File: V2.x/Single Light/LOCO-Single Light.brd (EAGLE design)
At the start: 25.1 x 16.8 mm, 49 parts, among them IC1 Atmega 328-P, IC2 MCP2515, IC3 MIC5219BM5, IC4 TP4056, IC5 DW01A, Q1 8MHz, Q2 16MHz, Q3 BSS123, Q4 FS8205ASOT-23-6L_TCP-L

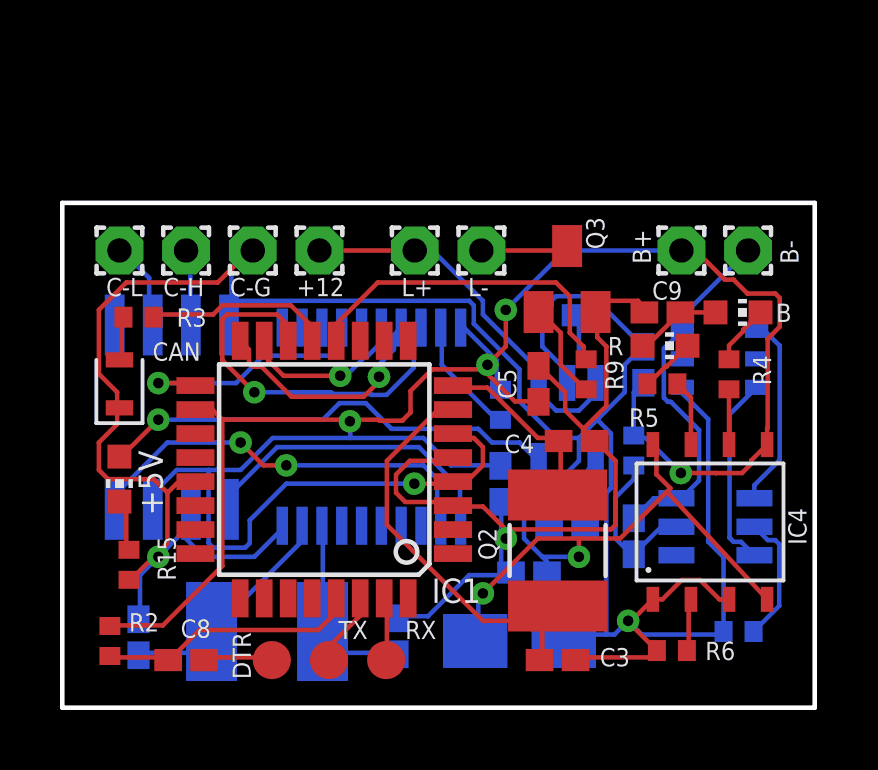
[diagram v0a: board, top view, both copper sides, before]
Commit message: new single light and single light akku versions
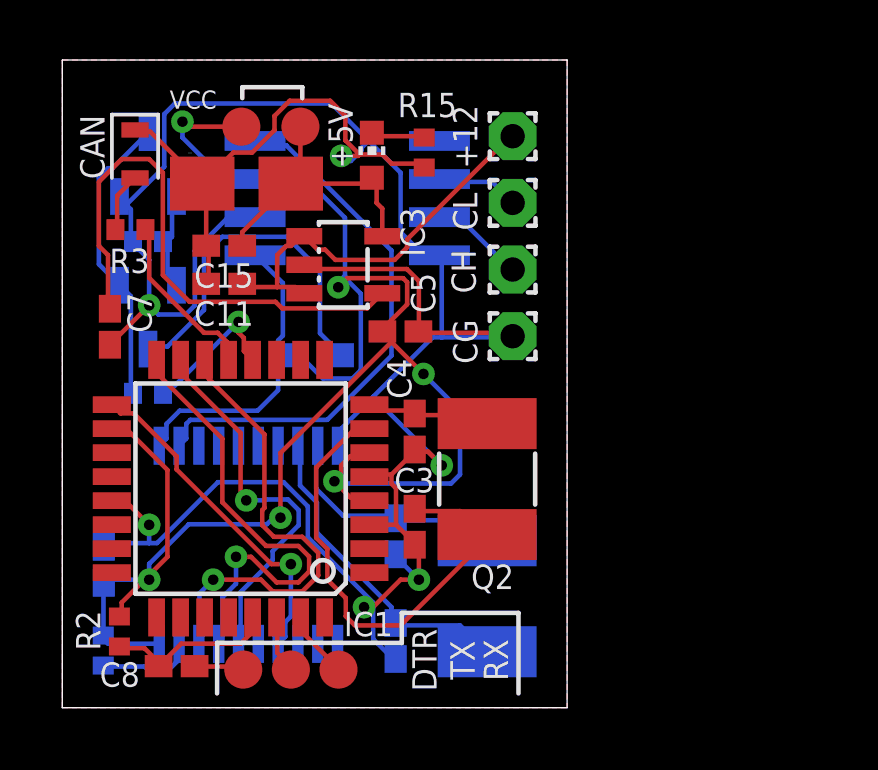
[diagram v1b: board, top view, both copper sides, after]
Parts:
- removed B, R: (no value), led:CHIP-LED0603
- removed B+, B-, C-G, C-H, C-L, L+, L-: (no value), wirepad:1,6/0,8
- removed C10: 0,1µ, rcl:C0402K
- removed C12: 10µ, rcl:C0402K
- removed C9: 100n, rcl:C0402K
- removed IC4: TP4056, TP4056:SOT23-8
- removed IC5: DW01A, DW01a:SOT23-6
- removed R5, R7: 1k, rcl:R0402
- removed R6: 1k2, rcl:R0402
- removed R8: 100R, rcl:R0402
- added 5V, VCC: PTR1B1,27, testpad:B1,27
- added CG, CH, CL: (no value), wirepad:1,6/0,8
- added LIGHT: (no value), led:CHIP-LED0603
- CAN: value LED1 -> CAN
- Q3: value BSS123 -> NPN; device transistor-small-signal:SOT23 -> Transistor:SOT95P237X112-3N
- Q4: value FS8205ASOT-23-6L_TCP-L -> NPN; device FS8205A:SOT-23-6L_TCP-L -> Transistor:SOT95P237X112-3N
- R4: value 1k -> 33
- moved R4 19.9 mm to (2.86, 15.5), flipped to the bottom, turned to 0 degrees
- moved Q4 19.1 mm to (2.86, 13.0), turned to 270 degrees
- moved C16 17.8 mm to (6.14, 17.5), flipped to the top
- moved R15 16.9 mm to (12.1, 18.5)
- moved C7 16.6 mm to (1.59, 12.7), flipped to the top, turned to 90 degrees
- moved R1 15.6 mm to (1.37, 1.91)
- moved C15 14.9 mm to (5.40, 15.4), flipped to the top, turned to 0 degrees
- moved R9 14.6 mm to (2.86, 10.5), flipped to the bottom, turned to 180 degrees
- moved Q3 14.5 mm to (2.86, 18.1), flipped to the bottom, turned to 90 degrees
- moved +5V 13.7 mm to (10.3, 18.4), turned to 0 degrees
- moved C6 13.5 mm to (1.39, 4.76), turned to 90 degrees
- moved C11 11.2 mm to (5.40, 14.1), flipped to the top, turned to 0 degrees
- moved DA1 9.36 mm to (9.50, 17.0), turned to 90 degrees
- moved C1 9.21 mm to (11.1, 5.71), turned to 270 degrees
- moved IC3 9.12 mm to (9.37, 14.8), flipped to the top, turned to 270 degrees
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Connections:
- removed net B-: B-.1, C10.1, IC5.6, Q4.3
- removed net LIGHT: L-.1, Q3.3
- removed net N$13: B.A, C9.2, R.A
- removed net N$14: IC5.3, Q4.6
- removed net N$16: IC5.1, Q4.4
- removed net N$17: C10.2, IC5.5, R8.2
- removed net N$18: IC5.2, R7.1
- removed net N$2: Q3.1, R9.1
- removed net N$8: IC4.7, R5.2
- removed net N$9: IC4.2, R6.2
- net +12V: no longer L+.1
- net +5V: now also 5V.TP; no longer IC4.4, IC4.8
- net CAN-H: now also CH.1; no longer C-H.1
- net CAN-L: now also CL.1; no longer C-L.1
- net GND: now also CG.1, R4.2; no longer C-G.1, C12.1, C9.1, IC4.1, IC4.3, Q4.1, R6.1, R7.2
- net N$4: now also Q3.1, Q4.2; no longer B.C
- net N$5: now also Q3.3, Q4.1, R9.1; no longer R.C, R5.1
- net N$7: now also LIGHT.C, Q4.3; no longer IC4.6, R4.2
- net VCC: now also LIGHT.A, VCC.TP; no longer B+.1, C12.2, IC4.5, R8.1
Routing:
- net +5V: track 37.6 -> 9.65 mm, vias 3 -> 0
- net GND: track 125.7 -> 98.1 mm, vias 3 -> 6
- net VCC: track 79.9 -> 62.3 mm, vias 5 -> 6
- net N$1: track 2.34 -> 18.4 mm
- net B-: track 12.1 -> 0.00 mm
- net N$7: track 1.84 -> 12.0 mm
- net N$5: track 1.86 -> 9.94 mm
- net SI: track 7.97 -> 16.0 mm
- net SO: track 5.69 -> 12.8 mm
- net D8: track 11.4 -> 4.96 mm, vias 0 -> 1
- net N$14: track 6.46 -> 0.00 mm
- net N$16: track 6.41 -> 0.00 mm
- net N$17: track 5.43 -> 0.00 mm
- net CAN-OCC2: track 6.39 -> 10.8 mm
- net N$18: track 4.34 -> 0.00 mm
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- added copper zone on layer 1, net GND
- added copper zone on layer 16, net GND
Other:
- board size 25.1 x 16.8 mm -> 16.8 x 21.6 mm
- board text added: "Single"
- board text added: "V2.2"
- board text added: "loco-can.github.io"
- board text removed: "LOCO-Single"
- board text removed: "V2.1-s"
